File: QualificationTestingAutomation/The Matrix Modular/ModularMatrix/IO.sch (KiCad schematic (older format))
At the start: 10 parts, among them J1 Conn_02x32_Counter_Clockwise_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, J5 Conn_02x32_Counter_Clockwise_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, J6 Banana Jack, J7 Banana Jack, J8 Banana Jack, J9 Banana Jack

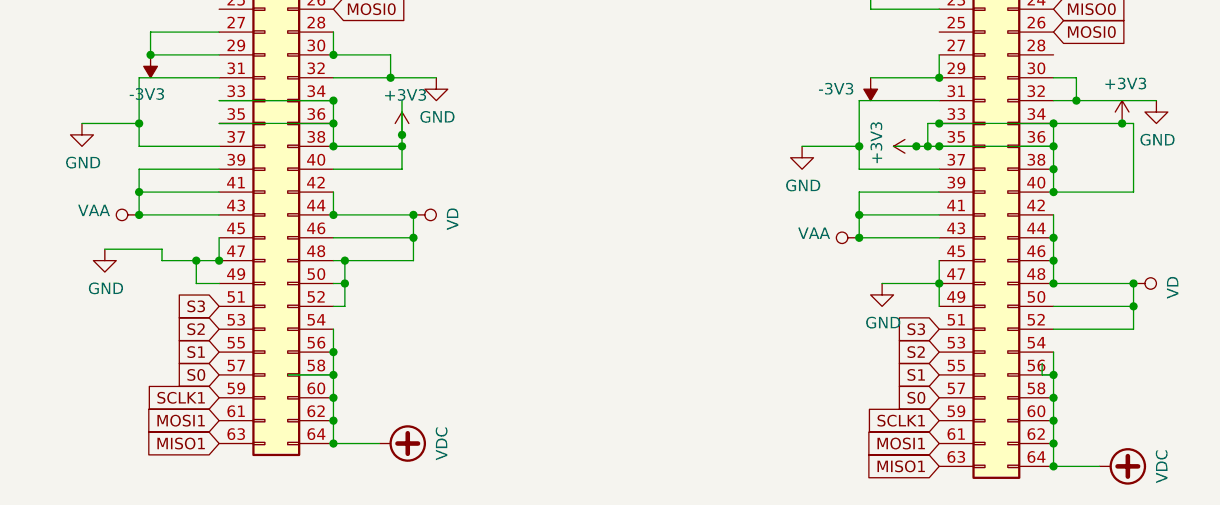
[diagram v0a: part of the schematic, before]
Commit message: Added Voltage and current measurment of the muxes and relays to the MSP Some clean up of the tracks.
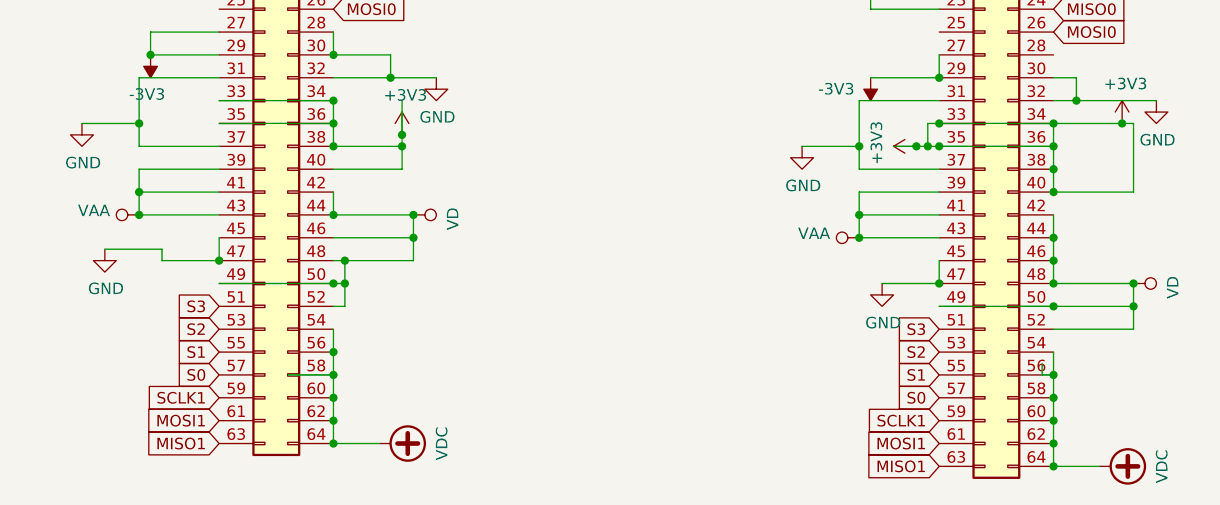
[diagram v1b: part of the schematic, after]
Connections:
- wire segments 197 -> 195
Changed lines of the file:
@@
 	2750 4300 2750 4400
-Wire Wire Line
-	2750 4400 2650 4400
 Wire Wire Line
 	2500 4400 2500 4350
 Wire Wire Line
 	5900 4400 5900 4500
-Wire Wire Line
-	2650 4400 2650 4500
-Wire Wire Line
-	2650 4500 2750 4500
-Connection ~ 2650 4400
-Wire Wire Line
-	2650 4400 2500 4400
-Wire Wire Line
-	5900 4600 5900 4500
 Connection ~ 5900 4500
 $Comp
@@
 	1    0    0    -1
 $EndComp
+Wire Wire Line
+	2500 4400 2750 4400
+Wire Wire Line
+	2750 4500 3250 4500
+Connection ~ 3250 4500
+Wire Wire Line
+	5900 4600 6400 4600
+Connection ~ 6400 4600
 $EndSCHEMATC
